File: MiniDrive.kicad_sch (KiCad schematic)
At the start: 22 parts, among them J1 Conn_LED, J2 Conn_24V, U1 TPS92200

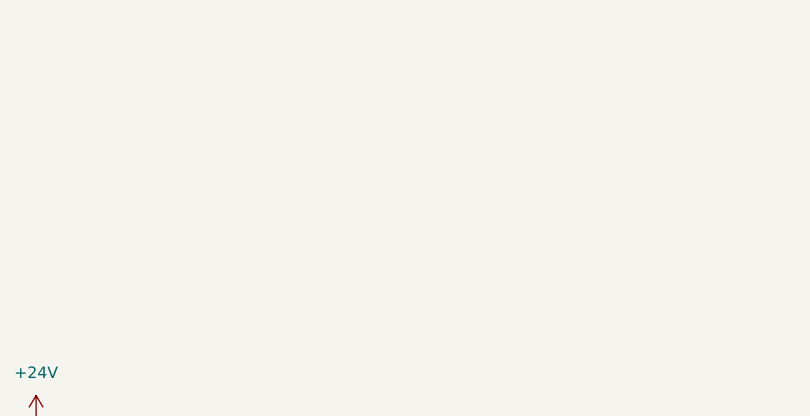
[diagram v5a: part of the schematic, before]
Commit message: Add power LED
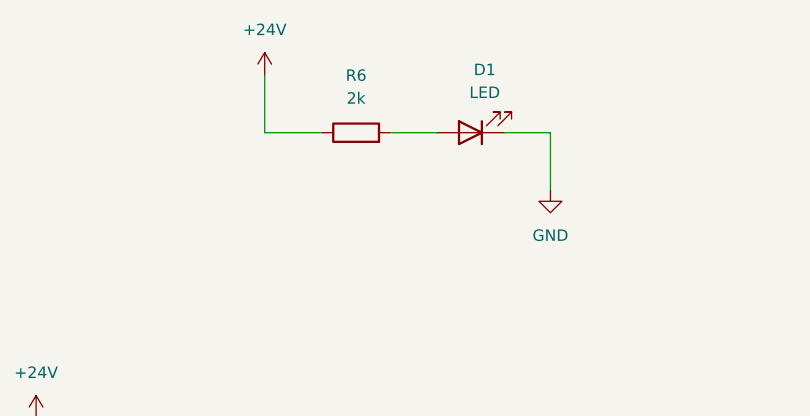
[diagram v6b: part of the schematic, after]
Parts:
- added D1: LED, LED_SMD:LED_0603_1608Metric, symbol Device:LED
- added R6: 2k, Resistor_SMD:R_0805_2012Metric, symbol Device:R
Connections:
- net +24V: now also R6.1
- net GND: now also D1.1 (K)
- new net: D1.2 (A), R6.2
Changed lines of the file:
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@@
+    (stroke (width 0) (type default))
+  )
+  (wire (pts (xy 140.97 31.75) (xy 146.05 31.75))
     (stroke (width 0) (type default))
   )
@@
     (stroke (width 0) (type default))
   )
+  (wire (pts (xy 114.3 25.4) (xy 114.3 31.75))
+    (stroke (width 0) (type default))
+  )
   (wire (pts (xy 158.75 76.2) (xy 165.1 76.2))
     (stroke (width 0) (type default))
@@
     (stroke (width 0) (type default))
   )
+  (wire (pts (xy 114.3 31.75) (xy 120.65 31.75))
+    (stroke (width 0) (type default))
+  )
   (wire (pts (xy 223.52 76.2) (xy 236.22 76.2))
     (stroke (width 0) (type default))
@@
     (stroke (width 0) (type default))
   )
+  (wire (pts (xy 146.05 31.75) (xy 146.05 38.1))
+    (stroke (width 0) (type default))
+  )
   (wire (pts (xy 80.01 95.25) (xy 101.6 95.25))
     (stroke (width 0) (type default))
@@
   )
   (wire (pts (xy 133.35 107.95) (xy 175.895 107.95))
+    (stroke (width 0) (type default))
+  )
+  (wire (pts (xy 128.27 31.75) (xy 133.35 31.75))
     (stroke (width 0) (type default))
   )
@@
     )
   )
+  (symbol (lib_id "Device:LED") (at 137.16 31.75 180) (unit 1)
+    (in_bom yes) (on_board yes) (dnp no) (fields_autoplaced)
+    (property "Reference" "D1" (at 138.7475 24.765 0)
+      (effects (font (size 1.27 1.27)))
+    )
+    (property "Value" "LED" (at 138.7475 27.305 0)
+      (effects (font (size 1.27 1.27)))
+    )
+    (property "Footprint" "LED_SMD:LED_0603_1608Metric" (at 137.16 31.75 0)
+      (effects (font (size 1.27 1.27)) hide)
+    )
+    (property "Datasheet" "~" (at 137.16 31.75 0)
+      (effects (font (size 1.27 1.27)) hide)
+    )
+    (pin "1")
+    (pin "2")
+    (instances
+      (project "MiniDrive"
+        (path "/e06caad1-a246-4f16-9d4f-053507cbe732"
+          (reference "D1") (unit 1)
+        )
+      )
+    )
+  )
   (symbol (lib_id "Device:C") (at 133.35 122.555 0) (unit 1)
     (in_bom yes) (on_board yes) (dnp yes) (fields_autoplaced)
@@
     )
   )
+  (symbol (lib_id "power:+24V") (at 114.3 25.4 0) (unit 1)
+    (in_bom yes) (on_board yes) (dnp no) (fields_autoplaced)
+    (property "Reference" "#PWR011" (at 114.3 29.21 0)
+      (effects (font (size 1.27 1.27)) hide)
+    )
+    (property "Value" "+24V" (at 114.3 20.32 0)
+      (effects (font (size 1.27 1.27)))
+    )
+    (property "Footprint" "" (at 114.3 25.4 0)
+      (effects (font (size 1.27 1.27)) hide)
+    )
+    (property "Datasheet" "" (at 114.3 25.4 0)
+      (effects (font (size 1.27 1.27)) hide)
+    )
+    (pin "1")
+    (instances
+      (project "MiniDrive"
+        (path "/e06caad1-a246-4f16-9d4f-053507cbe732"
+          (reference "#PWR011") (unit 1)
+        )
+      )
+    )
+  )
   (symbol (lib_id "Connector:TestPoint") (at 80.01 76.2 90) (unit 1)
     (in_bom yes) (on_board yes) (dnp no) (fields_autoplaced)
@@
         (path "/e06caad1-a246-4f16-9d4f-053507cbe732"
           (reference "#PWR05") (unit 1)
+        )
+      )
+    )
+  )
+  (symbol (lib_id "Device:R") (at 124.46 31.75 90) (unit 1)
+    (in_bom yes) (on_board yes) (dnp no) (fields_autoplaced)
+    (property "Reference" "R6" (at 124.46 25.4 90)
+      (effects (font (size 1.27 1.27)))
+    )
+    (property "Value" "2k" (at 124.46 27.94 90)
+      (effects (font (size 1.27 1.27)))
+    )
+    (property "Footprint" "Resistor_SMD:R_0805_2012Metric" (at 124.46 33.528 90)
+      (effects (font (size 1.27 1.27)) hide)
+    )
+    (property "Datasheet" "~" (at 124.46 31.75 0)
+      (effects (font (size 1.27 1.27)) hide)
+    )
+    (pin "1")
+    (pin "2")
+    (instances
+      (project "MiniDrive"
+        (path "/e06caad1-a246-4f16-9d4f-053507cbe732"
+          (reference "R6") (unit 1)
         )
       )
@@
         )
       )
+    )
+  )
+  (symbol (lib_id "power:GND") (at 146.05 38.1 0) (unit 1)
+    (in_bom yes) (on_board yes) (dnp no) (fields_autoplaced)
+    (property "Reference" "#PWR012" (at 146.05 44.45 0)
+      (effects (font (size 1.27 1.27)) hide)
+    )
+    (property "Value" "GND" (at 146.05 43.18 0)
+      (effects (font (size 1.27 1.27)))
+    )
+    (property "Footprint" "" (at 146.05 38.1 0)
+      (effects (font (size 1.27 1.27)) hide)
+    )
+    (property "Datasheet" "" (at 146.05 38.1 0)
+      (effects (font (size 1.27 1.27)) hide)
+    )
+    (pin "1")
+    (instances
+      (project "MiniDrive"
+        (path "/e06caad1-a246-4f16-9d4f-053507cbe732"
+          (reference "#PWR012") (unit 1)
+        )
+      )

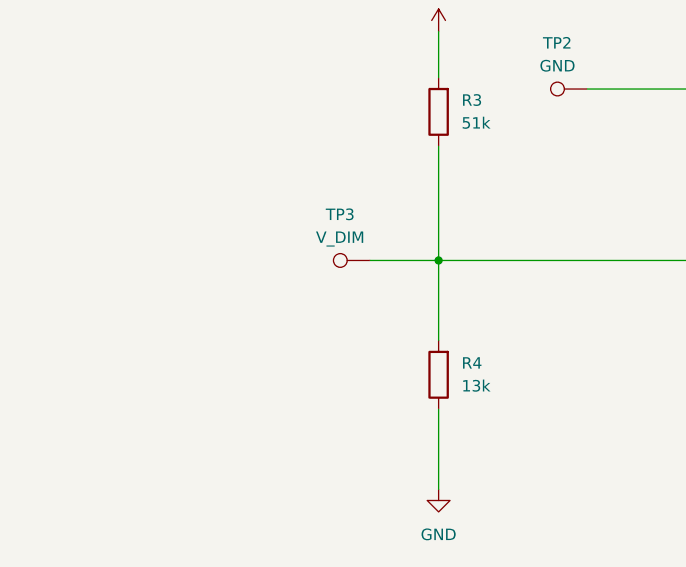
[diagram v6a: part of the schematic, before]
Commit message: Add off-board dimming connector
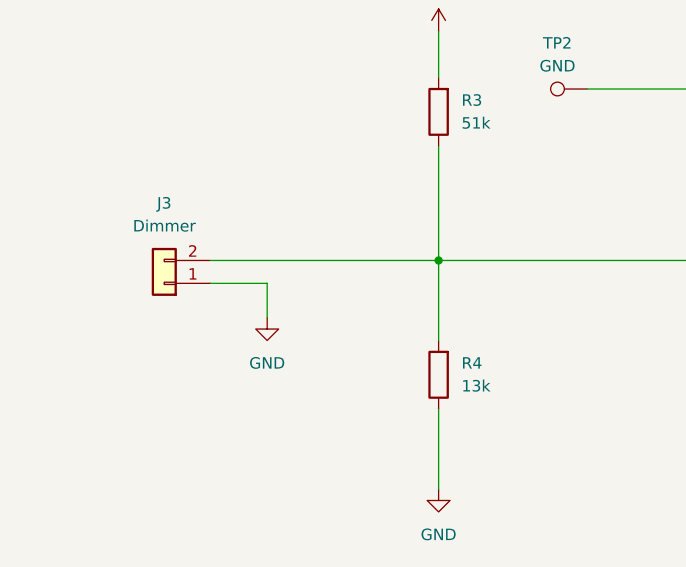
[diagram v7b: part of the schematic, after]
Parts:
- removed TP3: V_DIM, TestPoint:TestPoint_THTPad_D1.5mm_Drill0.7mm, symbol Connector:TestPoint
- added J3: Dimmer, Connector_JST:JST_PH_B2B-PH-K_1x02_P2.00mm_Vertical, symbol Connector_Generic:Conn_01x02
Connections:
- net GND: now also J3.1 (Pin_1)
- net at R3.1, R4.2, U1.2 (DIM): now also J3.2 (Pin_2)
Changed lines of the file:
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@@
-    (stroke (width 0) (type default))
-  )
-  (wire (pts (xy 55.88 114.3) (xy 63.5 114.3))
     (stroke (width 0) (type default))
   )
@@
     (stroke (width 0) (type default))
   )
+  (wire (pts (xy 38.1 114.3) (xy 63.5 114.3))
+    (stroke (width 0) (type default))
+  )
   (wire (pts (xy 63.5 114.3) (xy 127 114.3))
     (stroke (width 0) (type default))
@@
     (stroke (width 0) (type default))
   )
+  (wire (pts (xy 44.45 116.84) (xy 38.1 116.84))
+    (stroke (width 0) (type default))
+  )
   (wire (pts (xy 183.515 107.95) (xy 209.55 107.95))
     (stroke (width 0) (type default))
@@
   )
   (wire (pts (xy 114.3 88.9) (xy 114.3 95.25))
+    (stroke (width 0) (type default))
+  )
+  (wire (pts (xy 44.45 120.65) (xy 44.45 116.84))
     (stroke (width 0) (type default))
   )
@@
     )
   )
+  (symbol (lib_id "power:GND") (at 44.45 120.65 0) (unit 1)
+    (in_bom yes) (on_board yes) (dnp no) (fields_autoplaced)
+    (property "Reference" "#PWR013" (at 44.45 127 0)
+      (effects (font (size 1.27 1.27)) hide)
+    )
+    (property "Value" "GND" (at 44.45 125.73 0)
+      (effects (font (size 1.27 1.27)))
+    )
+    (property "Footprint" "" (at 44.45 120.65 0)
+      (effects (font (size 1.27 1.27)) hide)
+    )
+    (property "Datasheet" "" (at 44.45 120.65 0)
+      (effects (font (size 1.27 1.27)) hide)
+    )
+    (pin "1")
+    (instances
+      (project "MiniDrive"
+        (path "/e06caad1-a246-4f16-9d4f-053507cbe732"
+          (reference "#PWR013") (unit 1)
+        )
+      )
+    )
+  )
   (symbol (lib_id "Device:R") (at 124.46 31.75 90) (unit 1)
     (in_bom yes) (on_board yes) (dnp no) (fields_autoplaced)
@@
     )
   )
+  (symbol (lib_id "Connector_Generic:Conn_01x02") (at 33.02 116.84 180) (unit 1)
+    (in_bom yes) (on_board yes) (dnp no) (fields_autoplaced)
+    (property "Reference" "J3" (at 33.02 107.95 0)
+      (effects (font (size 1.27 1.27)))
+    )
+    (property "Value" "Dimmer" (at 33.02 110.49 0)
+      (effects (font (size 1.27 1.27)))
+    )
+    (property "Footprint" "Connector_JST:JST_PH_B2B-PH-K_1x02_P2.00mm_Vertical" (at 33.02 116.84 0)
+      (effects (font (size 1.27 1.27)) hide)
+    )
+    (property "Datasheet" "~" (at 33.02 116.84 0)
+      (effects (font (size 1.27 1.27)) hide)
+    )
+    (pin "1")
+    (pin "2")
+    (instances
+      (project "MiniDrive"
+        (path "/e06caad1-a246-4f16-9d4f-053507cbe732"
+          (reference "J3") (unit 1)
+        )
+      )
+    )
+  )
   (symbol (lib_id "Device:R") (at 63.5 127 180) (unit 1)
     (in_bom yes) (on_board yes) (dnp no) (fields_autoplaced)
@@
         )
       )
-    )
-  )
-  (symbol (lib_id "Connector:TestPoint") (at 55.88 114.3 90) (unit 1)
-    (in_bom yes) (on_board yes) (dnp no) (fields_autoplaced)
-    (property "Reference" "TP3" (at 52.578 109.22 90)
-      (effects (font (size 1.27 1.27)))
-    )
-    (property "Value" "V_DIM" (at 52.578 111.76 90)
-      (effects (font (size 1.27 1.27)))
-    )
-    (property "Footprint" "TestPoint:TestPoint_THTPad_D1.5mm_Drill0.7mm" (at 55.88 109.22 0)
-      (effects (font (size 1.27 1.27)) hide)
-    )
-    (property "Datasheet" "~" (at 55.88 109.22 0)
-      (effects (font (size 1.27 1.27)) hide)
-    )
-    (pin "1")
-    (instances
-      (project "MiniDrive"
-        (path "/e06caad1-a246-4f16-9d4f-053507cbe732"
-          (reference "TP3") (unit 1)
-        )
-      )

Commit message: Change mounting holes to M3
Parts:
- H1, H2: footprint MountingHole:MountingHole_2.7mm_M2.5 -> MountingHole:MountingHole_3.2mm_M3
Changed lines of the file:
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@@
       (effects (font (size 1.27 1.27)) (justify left))
     )
-    (property "Footprint" "MountingHole:MountingHole_2.7mm_M2.5" (at 25.4 182.88 0)
+    (property "Footprint" "MountingHole:MountingHole_3.2mm_M3" (at 25.4 182.88 0)
       (effects (font (size 1.27 1.27)) hide)
     )
@@
       (effects (font (size 1.27 1.27)) (justify left))
     )
-    (property "Footprint" "MountingHole:MountingHole_2.7mm_M2.5" (at 25.4 187.96 0)
-      (effects (font (size 1.27 1.27)) hide)
-    )
+    (property "Footprint" "MountingHole:MountingHole_3.2mm_M3" (at 25.4 187.96 0)
+      (effects (font (size 1.27 1.27)) hide)
+    )
